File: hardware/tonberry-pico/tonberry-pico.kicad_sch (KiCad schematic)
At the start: 5 parts, among them J1 MicroSD_Breakout, J2 I2SAudio_Breakout, J3 RC522_Breakout, U1 Pico

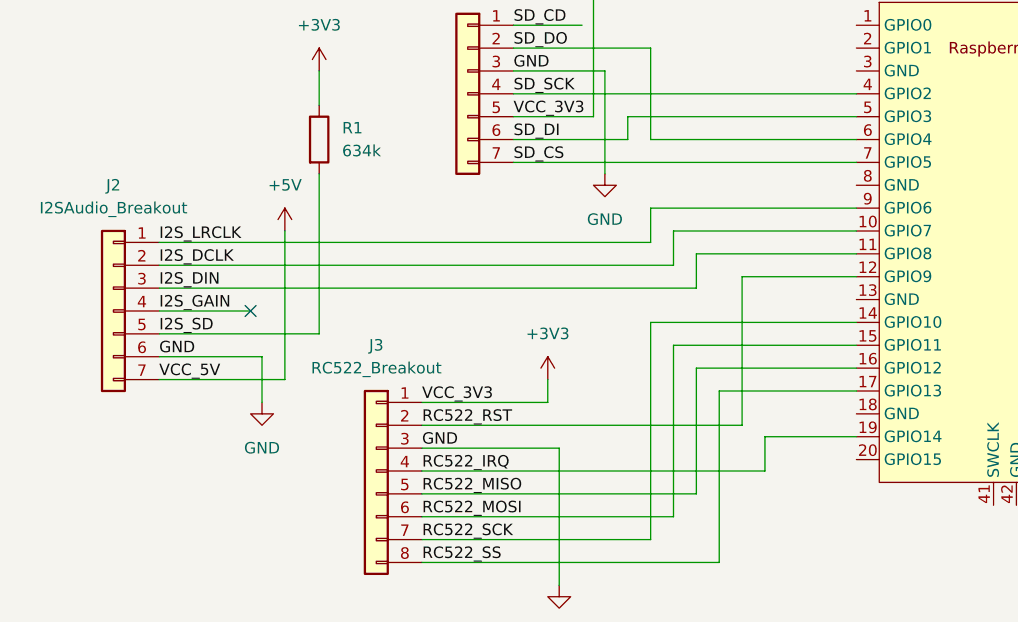
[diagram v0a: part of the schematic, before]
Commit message: Swap I2S LRCLK and DCLK for compatibility with micropython I2S
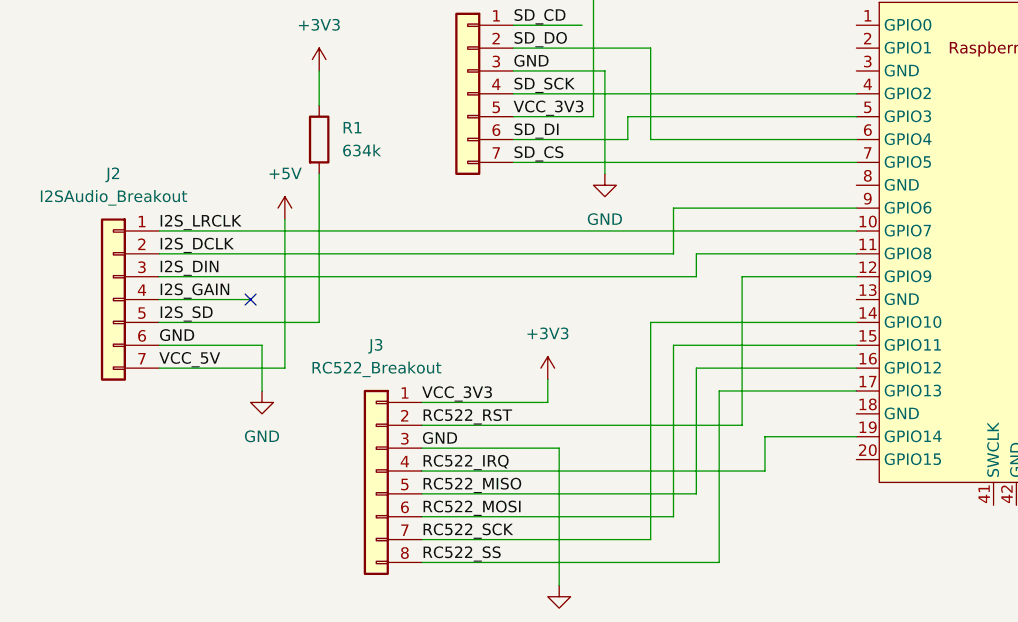
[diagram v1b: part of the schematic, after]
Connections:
- net I2S_DCLK: now also U1.9 (GPIO6); no longer U1.10 (GPIO7)
- net I2S_LRCLK: now also U1.10 (GPIO7); no longer U1.9 (GPIO6)
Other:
- moved on the sheet: J2
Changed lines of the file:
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@@
 	(paper "A4")
 	(no_connect
-		(at 41.91 91.44)
+		(at 41.91 90.17)
 	)
 	(wire
@@
 	(wire
 		(pts
-			(xy 31.75 91.44) (xy 41.91 91.44)
+			(xy 31.75 90.17) (xy 41.91 90.17)
 		)
 		(stroke
@@
 	(wire
 		(pts
-			(xy 91.44 85.09) (xy 91.44 88.9)
+			(xy 91.44 85.09) (xy 91.44 87.63)
 		)
 		(stroke
@@
 	(wire
 		(pts
-			(xy 31.75 86.36) (xy 88.9 86.36)
+			(xy 31.75 85.09) (xy 88.9 85.09)
 		)
 		(stroke
@@
 	(wire
 		(pts
-			(xy 45.72 99.06) (xy 45.72 82.55)
+			(xy 45.72 97.79) (xy 45.72 81.28)
 		)
 		(stroke
@@
 	(wire
 		(pts
-			(xy 31.75 88.9) (xy 91.44 88.9)
-		)
-		(stroke
-			(width 0)
-			(type default)
-		)
-	)
-	(wire
-		(pts
-			(xy 88.9 86.36) (xy 88.9 82.55)
-		)
-		(stroke
-			(width 0)
-			(type default)
-		)
-	)
-	(wire
-		(pts
-			(xy 31.75 93.98) (xy 49.53 93.98)
+			(xy 31.75 87.63) (xy 91.44 87.63)
+		)
+		(stroke
+			(width 0)
+			(type default)
+		)
+	)
+	(wire
+		(pts
+			(xy 31.75 92.71) (xy 49.53 92.71)
 		)
 		(stroke
@@
 	(wire
 		(pts
-			(xy 31.75 96.52) (xy 43.18 96.52)
+			(xy 31.75 95.25) (xy 43.18 95.25)
 		)
 		(stroke
@@
 	(wire
 		(pts
+			(xy 88.9 80.01) (xy 109.22 80.01)
+		)
+		(stroke
+			(width 0)
+			(type default)
+		)
+	)
+	(wire
+		(pts
 			(xy 109.22 95.25) (xy 88.9 95.25)
 		)
@@
 	(wire
 		(pts
-			(xy 88.9 82.55) (xy 109.22 82.55)
-		)
-		(stroke
-			(width 0)
-			(type default)
-		)
-	)
-	(wire
-		(pts
 			(xy 86.36 92.71) (xy 109.22 92.71)
 		)
@@
 	(wire
 		(pts
-			(xy 31.75 83.82) (xy 86.36 83.82)
+			(xy 31.75 82.55) (xy 109.22 82.55)
 		)
 		(stroke
@@
 	(wire
 		(pts
+			(xy 88.9 85.09) (xy 88.9 80.01)
+		)
+		(stroke
+			(width 0)
+			(type default)
+		)
+	)
+	(wire
+		(pts
 			(xy 109.22 69.85) (xy 83.82 69.85)
 		)
@@
 	(wire
 		(pts
-			(xy 31.75 99.06) (xy 45.72 99.06)
+			(xy 31.75 97.79) (xy 45.72 97.79)
 		)
 		(stroke
@@
 	(wire
 		(pts
-			(xy 109.22 80.01) (xy 86.36 80.01)
-		)
-		(stroke
-			(width 0)
-			(type default)
-		)
-	)
-	(wire
-		(pts
-			(xy 86.36 80.01) (xy 86.36 83.82)
-		)
-		(stroke
-			(width 0)
-			(type default)
-		)
-	)
-	(wire
-		(pts
 			(xy 60.96 116.84) (xy 86.36 116.84)
 		)
@@
 	(wire
 		(pts
-			(xy 49.53 76.2) (xy 49.53 93.98)
+			(xy 49.53 76.2) (xy 49.53 92.71)
 		)
 		(stroke
@@
 	(wire
 		(pts
-			(xy 43.18 101.6) (xy 43.18 96.52)
+			(xy 43.18 100.33) (xy 43.18 95.25)
 		)
 		(stroke
@@
 	)
 	(label "I2S_LRCLK"
-		(at 31.75 83.82 0)
+		(at 31.75 82.55 0)
 		(fields_autoplaced yes)
 		(effects
@@
 	)
 	(label "GND"
-		(at 31.75 96.52 0)
+		(at 31.75 95.25 0)
 		(fields_autoplaced yes)
 		(effects
@@
 	)
 	(label "I2S_GAIN"
-		(at 31.75 91.44 0)
+		(at 31.75 90.17 0)
 		(fields_autoplaced yes)
 		(effects
@@
 	)
 	(label "I2S_DIN"
-		(at 31.75 88.9 0)
+		(at 31.75 87.63 0)
 		(fields_autoplaced yes)
 		(effects
@@
 	)
 	(label "VCC_5V"
-		(at 31.75 99.06 0)
+		(at 31.75 97.79 0)
 		(fields_autoplaced yes)
 		(effects
@@
 	)
 	(label "I2S_SD"
-		(at 31.75 93.98 0)
+		(at 31.75 92.71 0)
 		(fields_autoplaced yes)
 		(effects
@@
 	)
 	(label "I2S_DCLK"
-		(at 31.75 86.36 0)
+		(at 31.75 85.09 0)
 		(fields_autoplaced yes)
 		(effects
@@
 	(symbol
 		(lib_id "power:+5V")
-		(at 45.72 82.55 0)
+		(at 45.72 81.28 0)
 		(unit 1)
 		(exclude_from_sim no)
@@
 		(fields_autoplaced yes)
 		(property "Reference" "#PWR06"
-			(at 45.72 86.36 0)
+			(at 45.72 85.09 0)
 			(effects
 				(font
@@
 		)
 		(property "Value" "+5V"
-			(at 45.72 77.47 0)
+			(at 45.72 76.2 0)
 			(effects
 				(font
@@
 		)
 		(property "Footprint" ""
-			(at 45.72 82.55 0)
+			(at 45.72 81.28 0)
 			(effects
 				(font
@@
 		)
 		(property "Datasheet" ""
-			(at 45.72 82.55 0)
+			(at 45.72 81.28 0)
 			(effects
 				(font
@@
 		)
 		(property "Description" "Power symbol creates a global label with name \"+5V\""
-			(at 45.72 82.55 0)
+			(at 45.72 81.28 0)
 			(effects
 				(font
@@
 	(symbol
 		(lib_id "power:GND")
-		(at 43.18 101.6 0)
+		(at 43.18 100.33 0)
 		(unit 1)
 		(exclude_from_sim no)
@@
 		(fields_autoplaced yes)
 		(property "Reference" "#PWR05"
-			(at 43.18 107.95 0)
+			(at 43.18 106.68 0)
 			(effects
 				(font
@@
 		)
 		(property "Value" "GND"
-			(at 43.18 106.68 0)
+			(at 43.18 105.41 0)
 			(effects
 				(font
@@
 		)
 		(property "Footprint" ""
-			(at 43.18 101.6 0)
+			(at 43.18 100.33 0)
 			(effects
 				(font
@@
 		)
 		(property "Datasheet" ""
-			(at 43.18 101.6 0)
+			(at 43.18 100.33 0)
 			(effects
 				(font
@@
 		)
 		(property "Description" "Power symbol creates a global label with name \"GND\" , ground"
-			(at 43.18 101.6 0)
+			(at 43.18 100.33 0)
 			(effects
 				(font
@@
 	(symbol
 		(lib_id "Connector_Generic:Conn_01x07")
-		(at 26.67 91.44 0)
+		(at 26.67 90.17 0)
 		(mirror y)
 		(unit 1)
@@
 		(fields_autoplaced yes)
 		(property "Reference" "J2"
-			(at 26.67 77.47 0)
+			(at 26.67 76.2 0)
 			(effects
 				(font
@@
 		)
 		(property "Value" "I2SAudio_Breakout"
-			(at 26.67 80.01 0)
+			(at 26.67 78.74 0)
 			(effects
 				(font
@@
 		)
 		(property "Footprint" ""
-			(at 26.67 91.44 0)
+			(at 26.67 90.17 0)
 			(effects
 				(font
@@
 		)
 		(property "Datasheet" "~"
-			(at 26.67 91.44 0)
+			(at 26.67 90.17 0)
 			(effects
 				(font
@@
 		)
 		(property "Description" "Generic connector, single row, 01x07, script generated (kicad-library-utils/schlib/autogen/connector/)"
-			(at 26.67 91.44 0)
-			(effects
-				(font
+			(at 26.67 90.17 0)
+			(effects
+				(font

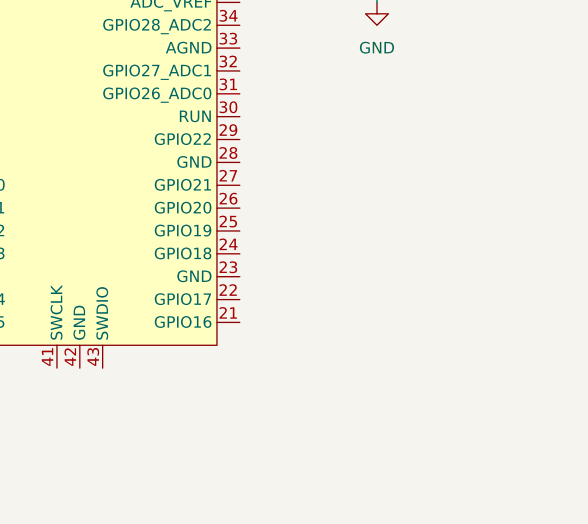
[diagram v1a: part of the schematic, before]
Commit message: schematic: Add WS2812 / Neopixel on GPIO16
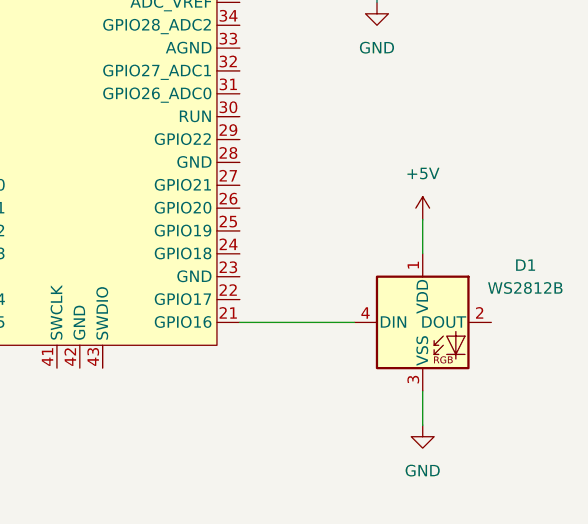
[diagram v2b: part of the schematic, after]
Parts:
- added D1: WS2812B, LED_SMD:LED_WS2812B_PLCC4_5.0x5.0mm_P3.2mm, symbol LED:WS2812B
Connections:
- net +5V: now also D1.1 (VDD)
- net GND: now also D1.3 (VSS)
- net at U1.21 (GPIO16): now also D1.4 (DIN)
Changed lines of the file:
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@@
+	(wire
+		(pts
+			(xy 144.78 107.95) (xy 157.48 107.95)
+		)
+		(stroke
+			(width 0)
+			(type default)
+		)
+	)
 	(wire
 		(pts
@@
 	(wire
 		(pts
+			(xy 165.1 96.52) (xy 165.1 100.33)
+		)
+		(stroke
+			(width 0)
+			(type default)
+		)
+	)
+	(wire
+		(pts
 			(xy 109.22 85.09) (xy 91.44 85.09)
 		)
@@
 		(pts
 			(xy 80.01 41.91) (xy 80.01 69.85)
+		)
+		(stroke
+			(width 0)
+			(type default)
+		)
+	)
+	(wire
+		(pts
+			(xy 165.1 115.57) (xy 165.1 119.38)
 		)
 		(stroke
@@
 		(on_board yes)
 		(dnp no)
-		(fields_autoplaced yes)
 		(property "Reference" "U1"
 			(at 127 52.07 0)
@@
 				(path "/7226ca0f-138a-46b4-89f3-dc32dfb1f9f7"
 					(reference "U1")
+					(unit 1)
+				)
+			)
+		)
+	)
+	(symbol
+		(lib_id "power:+5V")
+		(at 165.1 96.52 0)
+		(unit 1)
+		(exclude_from_sim no)
+		(in_bom yes)
+		(on_board yes)
+		(dnp no)
+		(fields_autoplaced yes)
+		(property "Reference" "#PWR011"
+			(at 165.1 100.33 0)
+			(effects
+				(font
+					(size 1.27 1.27)
+				)
+				(hide yes)
+			)
+		)
+		(property "Value" "+5V"
+			(at 165.1 91.44 0)
+			(effects
+				(font
+					(size 1.27 1.27)
+				)
+			)
+		)
+		(property "Footprint" ""
+			(at 165.1 96.52 0)
+			(effects
+				(font
+					(size 1.27 1.27)
+				)
+				(hide yes)
+			)
+		)
+		(property "Datasheet" ""
+			(at 165.1 96.52 0)
+			(effects
+				(font
+					(size 1.27 1.27)
+				)
+				(hide yes)
+			)
+		)
+		(property "Description" "Power symbol creates a global label with name \"+5V\""
+			(at 165.1 96.52 0)
+			(effects
+				(font
+					(size 1.27 1.27)
+				)
+				(hide yes)
+			)
+		)
+		(pin "1"
+		)
+		(instances
+			(project "tonberry-pico"
+				(path "/7226ca0f-138a-46b4-89f3-dc32dfb1f9f7"
+					(reference "#PWR011")
 					(unit 1)
 				)
@@
 	)
 	(symbol
+		(lib_id "LED:WS2812B")
+		(at 165.1 107.95 0)
+		(unit 1)
+		(exclude_from_sim no)
+		(in_bom yes)
+		(on_board yes)
+		(dnp no)
+		(fields_autoplaced yes)
+		(property "Reference" "D1"
+			(at 176.53 101.6314 0)
+			(effects
+				(font
+					(size 1.27 1.27)
+				)
+			)
+		)
+		(property "Value" "WS2812B"
+			(at 176.53 104.1714 0)
+			(effects
+				(font
+					(size 1.27 1.27)
+				)
+			)
+		)
+		(property "Footprint" "LED_SMD:LED_WS2812B_PLCC4_5.0x5.0mm_P3.2mm"
+			(at 166.37 115.57 0)
+			(effects
+				(font
+					(size 1.27 1.27)
+				)
+				(justify left top)
+				(hide yes)
+			)
+		)
+		(property "Datasheet" "https://cdn-shop.adafruit.com/datasheets/WS2812B.pdf"
+			(at 167.64 117.475 0)
+			(effects
+				(font
+					(size 1.27 1.27)
+				)
+				(justify left top)
+				(hide yes)
+			)
+		)
+		(property "Description" "RGB LED with integrated controller"
+			(at 165.1 107.95 0)
+			(effects
+				(font
+					(size 1.27 1.27)
+				)
+				(hide yes)
+			)
+		)
+		(pin "2"
+		)
+		(pin "1"
+		)
+		(pin "3"
+		)
+		(pin "4"
+		)
+		(instances
+			(project "tonberry-pico"
+				(path "/7226ca0f-138a-46b4-89f3-dc32dfb1f9f7"
+					(reference "D1")
+					(unit 1)
+				)
+			)
+		)
+	)
+	(symbol
 		(lib_id "power:GND")
 		(at 160.02 72.39 0)
@@
 					(unit 1)
 				)
+			)
+		)
+	)
+	(symbol
+		(lib_id "power:GND")
+		(at 165.1 119.38 0)
+		(unit 1)
+		(exclude_from_sim no)
+		(in_bom yes)
+		(on_board yes)
+		(dnp no)
+		(fields_autoplaced yes)
+		(property "Reference" "#PWR012"
+			(at 165.1 125.73 0)
+			(effects
+				(font
+					(size 1.27 1.27)
+				)
+				(hide yes)
+			)
+		)
+		(property "Value" "GND"
+			(at 165.1 124.46 0)
+			(effects
+				(font
+					(size 1.27 1.27)
+				)
+			)
+		)
+		(property "Footprint" ""
+			(at 165.1 119.38 0)
+			(effects
+				(font
+					(size 1.27 1.27)
+				)
+				(hide yes)
+			)
+		)
+		(property "Datasheet" ""
+			(at 165.1 119.38 0)
+			(effects
+				(font
+					(size 1.27 1.27)
+				)
+				(hide yes)
+			)
+		)
+		(property "Description" "Power symbol creates a global label with name \"GND\" , ground"
+			(at 165.1 119.38 0)
+			(effects
+				(font
+					(size 1.27 1.27)
+				)
+				(hide yes)
+			)
+		)
+		(pin "1"
+		)
+		(instances
+			(project "tonberry-pico"
+				(path "/7226ca0f-138a-46b4-89f3-dc32dfb1f9f7"
+					(reference "#PWR012")
+					(unit 1)
+				)

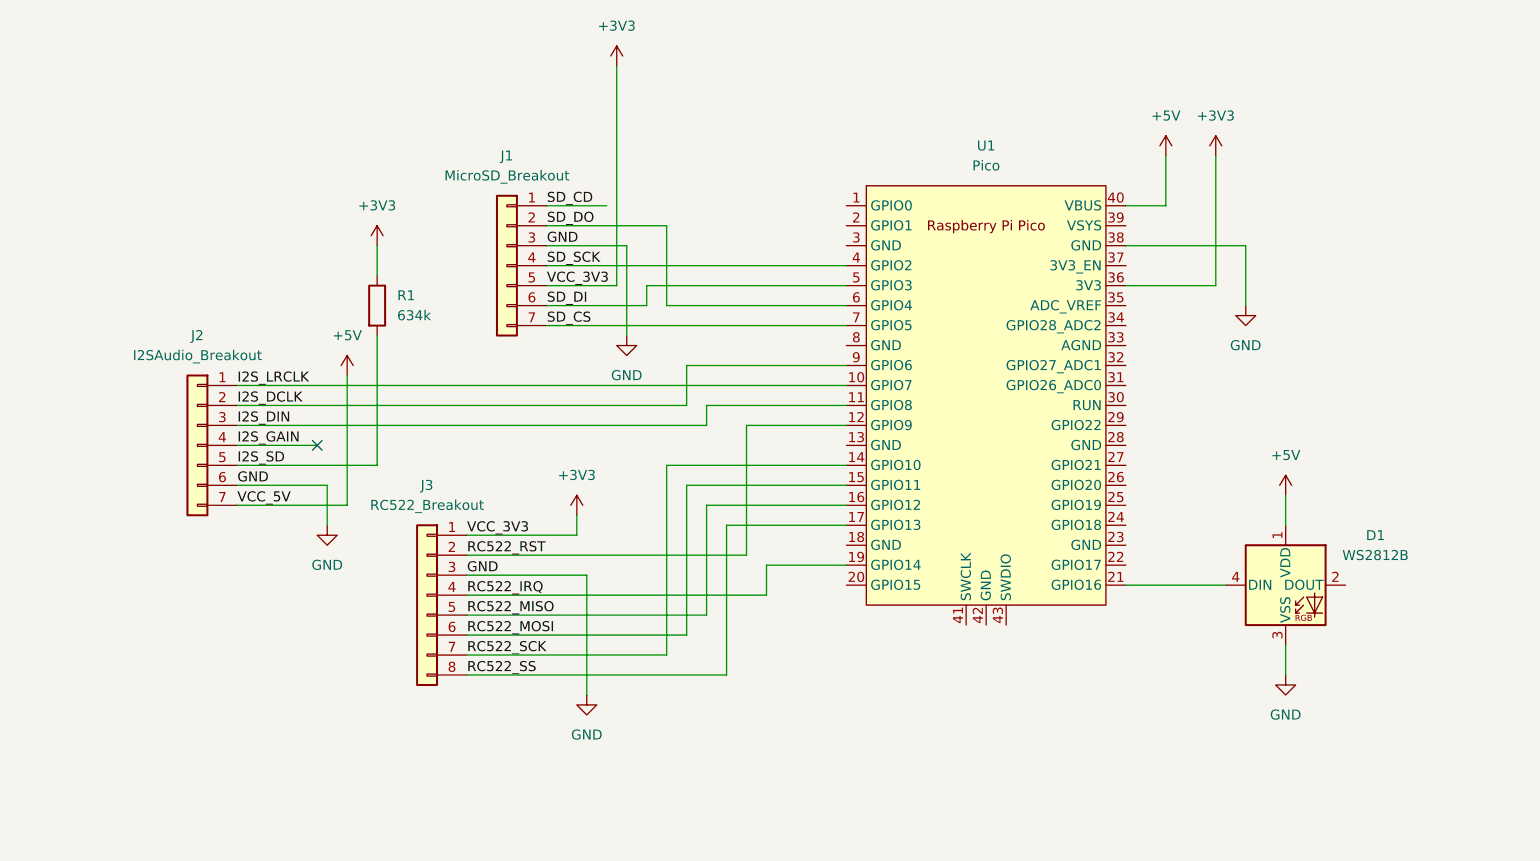
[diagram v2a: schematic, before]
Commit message: schematic: Update to KiCad 9 and some minor fixes
- Add gain setting resistor for I2S Amp
- Add three pushbuttons
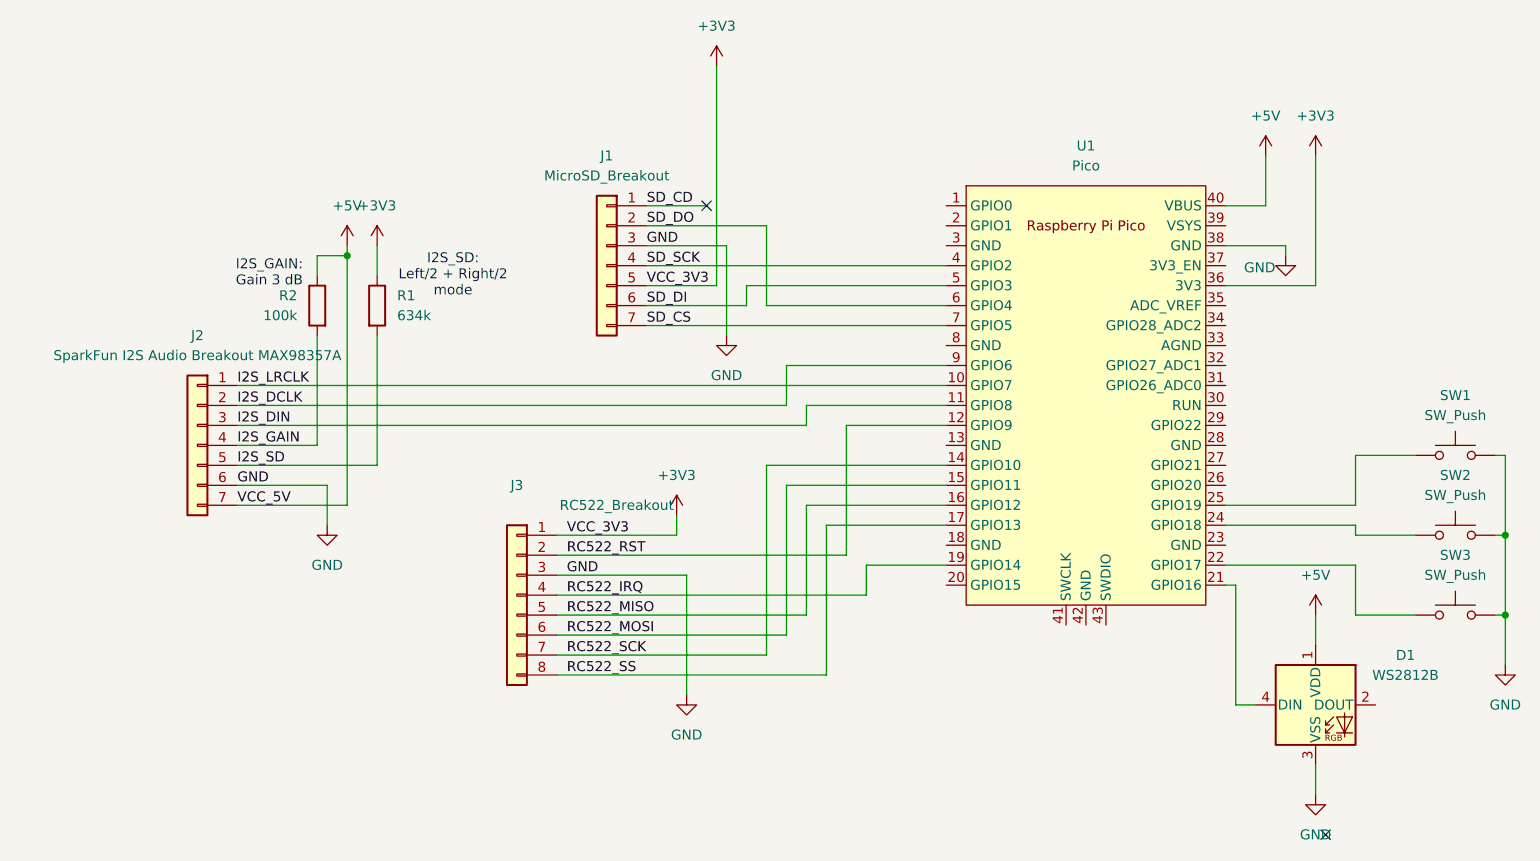
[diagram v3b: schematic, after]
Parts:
- added R2: 100k, symbol Device:R
- added SW1, SW2, SW3: SW_Push, symbol Switch:SW_Push
- J2: value I2SAudio_Breakout -> SparkFun I2S Audio Breakout MAX98357A
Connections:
- net +5V: now also R2.1
- net GND: now also SW1.2, SW2.2, SW3.2
- net I2S_GAIN: now also R2.2
- net at U1.22 (GPIO17): now also SW3.1
- net at U1.24 (GPIO18): now also SW2.1
- net at U1.25 (GPIO19): now also SW1.1
- no-connect marks 1 -> 2
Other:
- note added: "I2S_GAIN: Gain 3 dB"
- note added: "I2S_SD: Left/2 + Right/2 mode"
- moved on the sheet: D1, J1, J3, U1
